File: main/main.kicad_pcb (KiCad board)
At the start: 2 copper layers, 45.1 x 52.6 mm, 36 parts, among them P2 CONN_5, P7 CONN_10, P8 CONN_7, U1 MKL03Z32VFK4, U2 IS31FL3737, U4 ESD

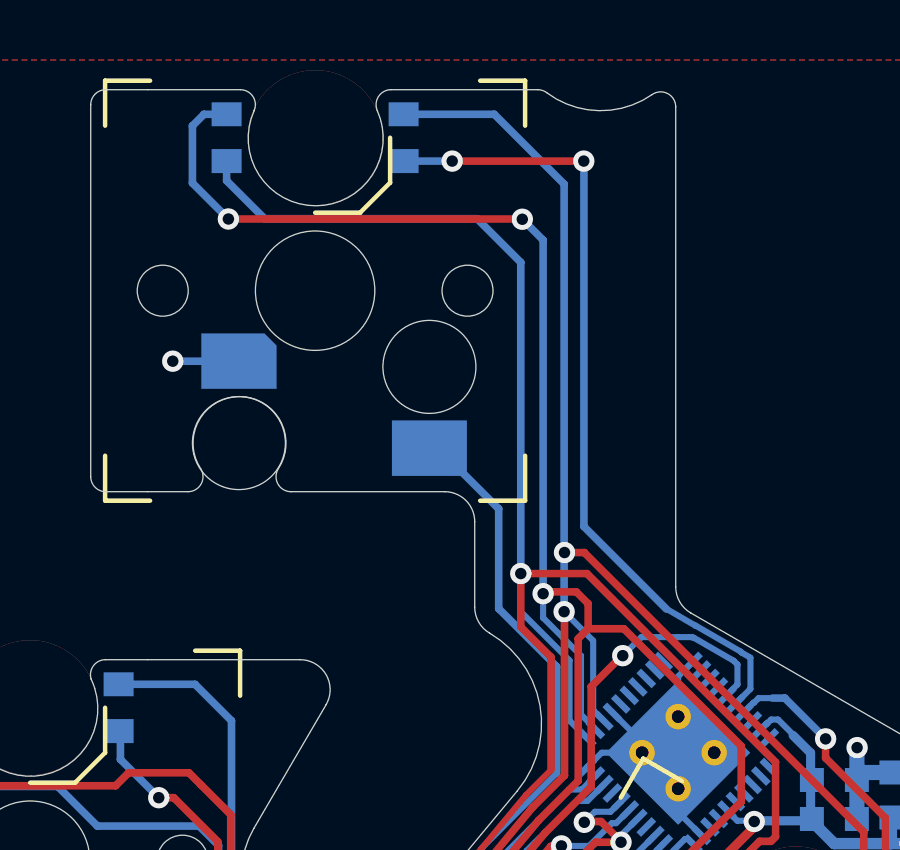
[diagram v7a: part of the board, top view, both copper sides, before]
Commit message: Add UHK logo.
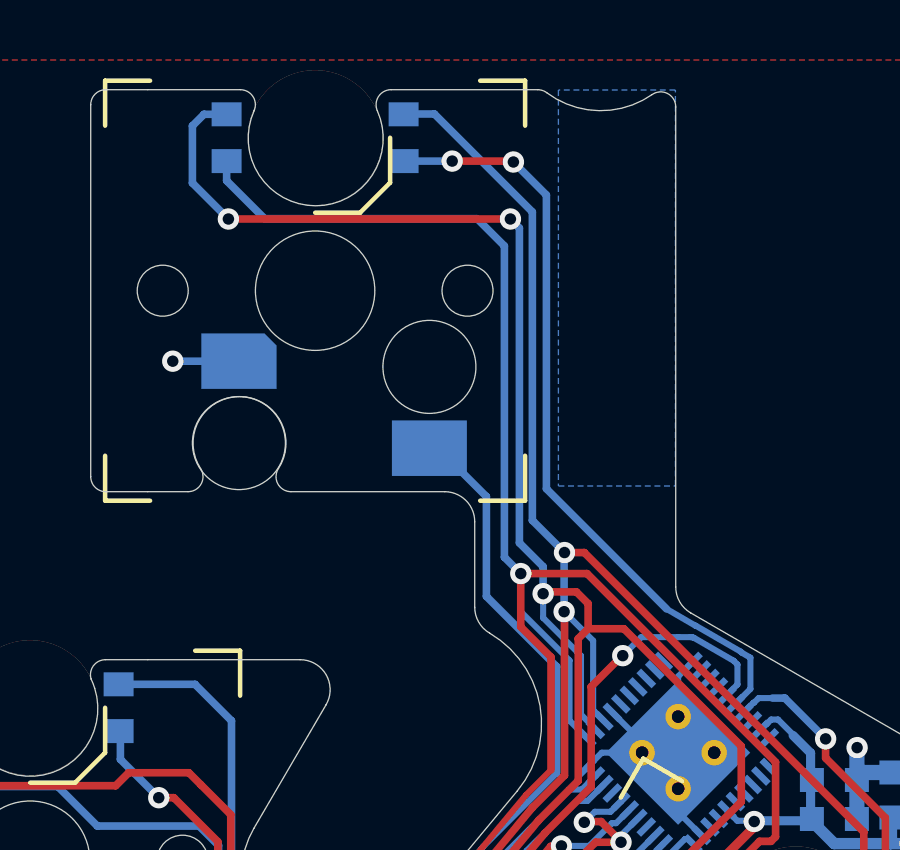
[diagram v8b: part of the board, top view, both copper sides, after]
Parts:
- added G***: LOGO, UGL:UHK_Logo_12x3.4_mm, B.Cu at (152.7, 88.1)
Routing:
- net /LED_CS2: track 27.0 -> 25.6 mm
- net /LED_SW3: track 72.7 -> 71.9 mm
- added copper zone on B.Cu, net (none)
